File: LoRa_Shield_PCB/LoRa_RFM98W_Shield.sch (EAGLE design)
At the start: 28 parts, among them IC1 AHT10, IC2 TXS0102DCUR, J2 TYPE-C-31-M-17, U1 RFM98W, U2 3V3_REG, X2 BU-SMA-H

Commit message: update
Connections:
- new net N$16: JP5.4
- new net N$8: JP5.3
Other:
- moved on the sheet: C5, C6, IC2, JP5

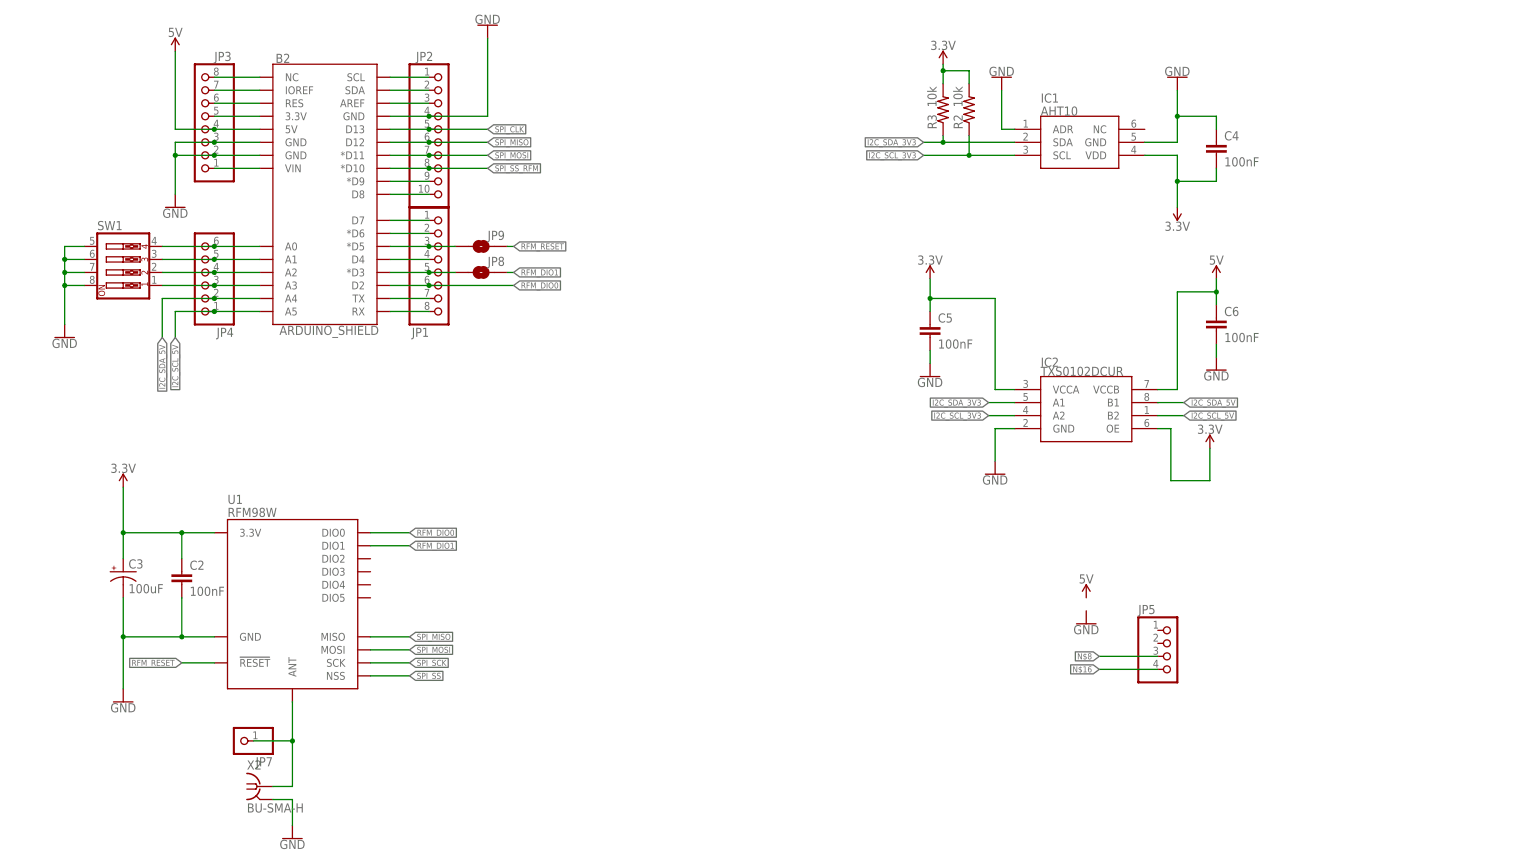
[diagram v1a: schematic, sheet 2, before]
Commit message: ADC circuit, new PCB layout
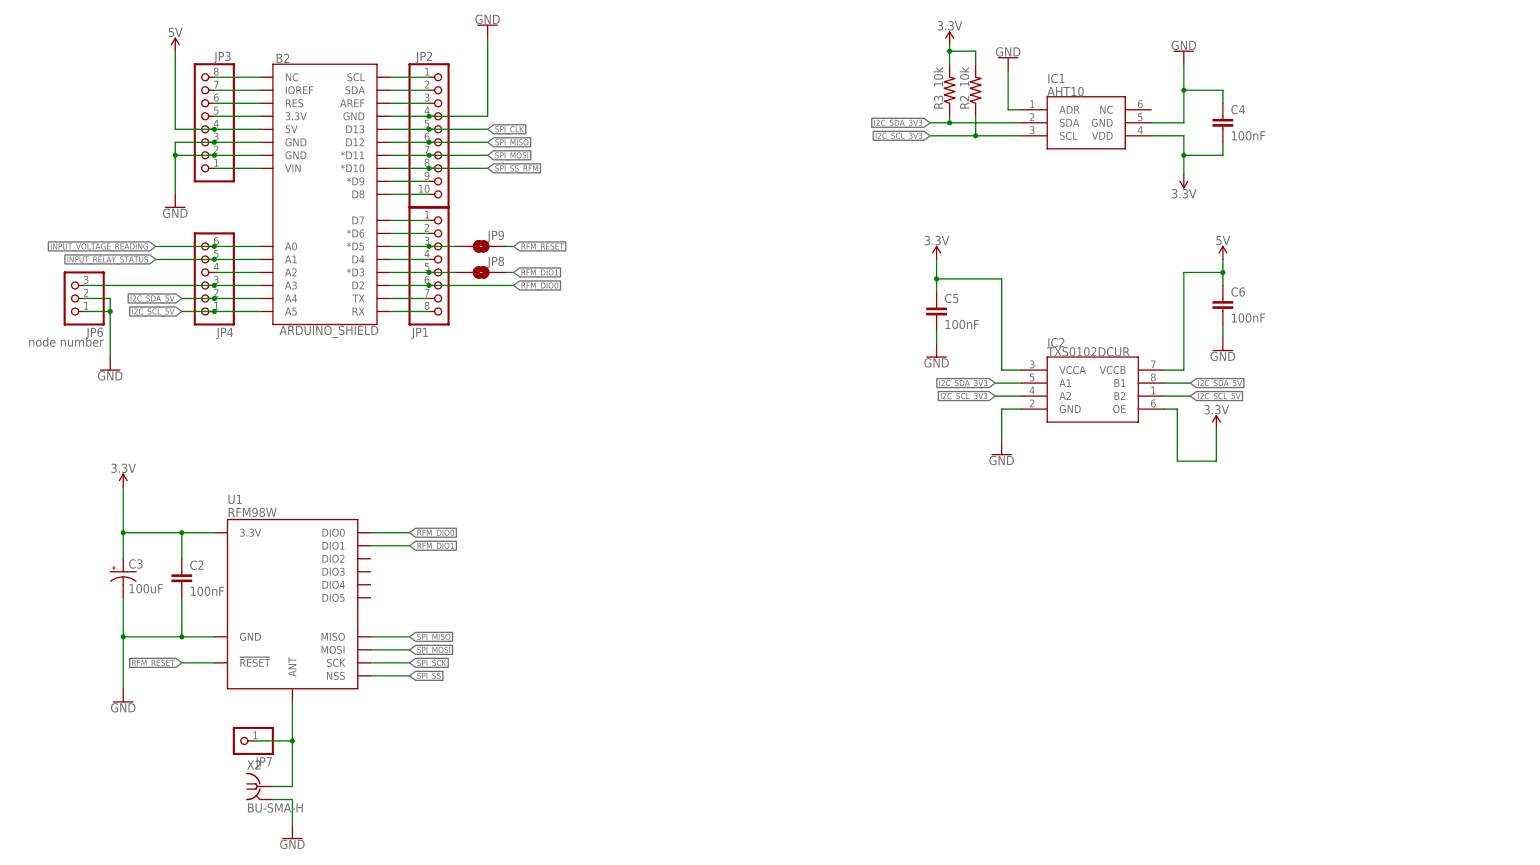
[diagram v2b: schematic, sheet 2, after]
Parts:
- removed SW1: (no value), special:SW_DIP-4
- added C7: 100nF, rcl:C-EUC0603
- added D2, D3: B5819W, dp_devices:DIODE-SOD-123
- added J1: CON_TERMINAL_BLOCK_03-5MM, dp_devices:CON_TERMINAL_BLOCK_03-5MM
- added JP6: node number, pinhead_v2:PINHD-1X3/OCT
- added R5, R7: 10k, rcl:R-US_R0603
- added R6: 150k, rcl:R-US_R0603
- JP5: value (none) -> OLED
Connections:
- removed net N$16: JP5.4
- removed net N$27: B2.A0, JP4.6, SW1.4
- removed net N$28: B2.A1, JP4.5, SW1.3
- new net INPUT_RELAY_STATUS: B2.A1, J1.1, JP4.5, R5.2
- new net INPUT_VOLTAGE_READING: B2.A0, C7.1, D2.A, D3.C, JP4.6, R6.1, R7.2
- net 5V: now also D2.C, JP5.1
- net GND: now also C7.2, D3.A, J1.2, JP5.2, JP6.1, JP6.2, R5.1, R7.1; no longer SW1.5, SW1.6, SW1.7, SW1.8
- net I2C_SCL_5V: now also JP5.3
- net I2C_SDA_5V: now also JP5.4
- net N$29: no longer SW1.2
- net N$30: now also JP6.3; no longer SW1.1
- net N$8: now also J1.3, R6.2; no longer JP5.3
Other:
- moved on the sheet: C1, C10, C4, C5, C6, D1, IC1, IC2, J2, LED1, R1, R2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

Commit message: layout update
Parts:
- removed D2, D3: B5819W, dp_devices:DIODE-SOD-123
- added D4: BAT54SWT1G, SamacSys_Parts:BAT54SWT1G
- added R10, R12, R8: 5k, rcl:R-US_R0603
- added R11, R4, R9: 10k, rcl:R-US_R0603
- R6: value 150k -> 165k
- R7: value 10k -> 15k
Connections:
- removed net SPI_CLK: B2.D13, JP2.5
- removed net SPI_MOSI: B2.*D11, JP2.7, U1.MOSI
- removed net SPI_SCK: U1.SCK
- removed net SPI_SS: U1.NSS
- removed net SPI_SS_RFM: B2.*D10, JP2.8
- new net SPI_CLK_3V3: R4.1, R8.2, U1.SCK
- new net SPI_CLK_5V: B2.D13, JP2.5, R8.1
- new net SPI_MOSI_3V3: R10.2, R9.1, U1.MOSI
- new net SPI_MOSI_5V: B2.*D11, JP2.7, R10.1
- new net SPI_SS_RFM_3V3: R11.1, R12.2, U1.NSS
- new net SPI_SS_RFM_5V: B2.*D10, JP2.8, R12.1
- net 5V: now also D4.CATHODE; no longer D2.C
- net GND: now also D4.ANODE, R11.2, R4.2, R9.2; no longer D3.A
- net INPUT_VOLTAGE_READING: now also D4.CATHODE-ANODE; no longer D2.A, D3.C
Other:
- moved on the sheet: C7, R6

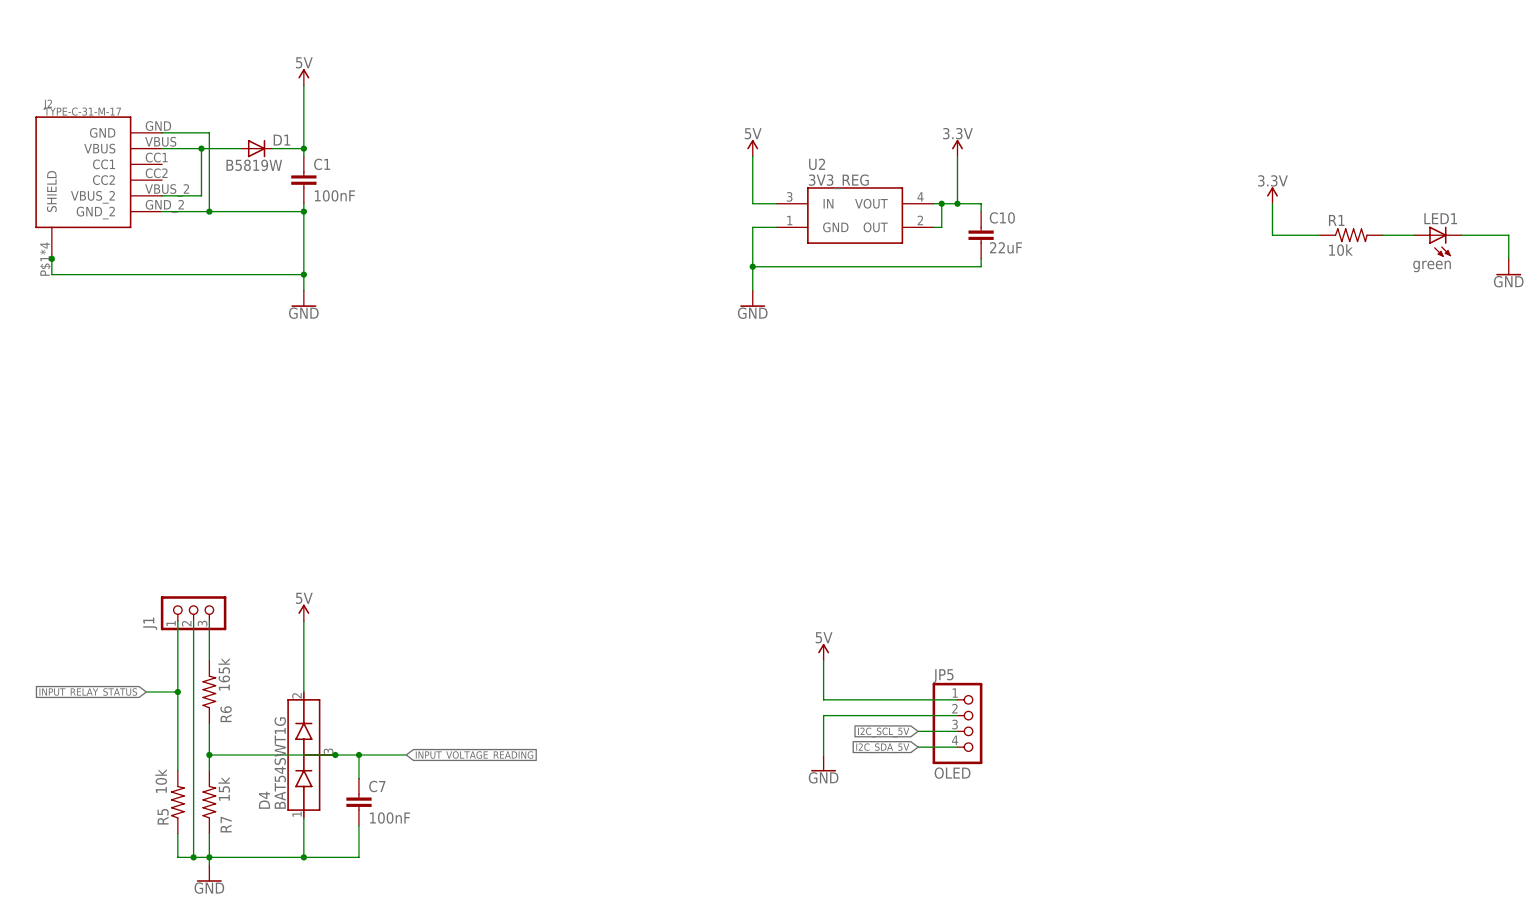
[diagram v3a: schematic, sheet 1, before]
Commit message: schematics, layout update
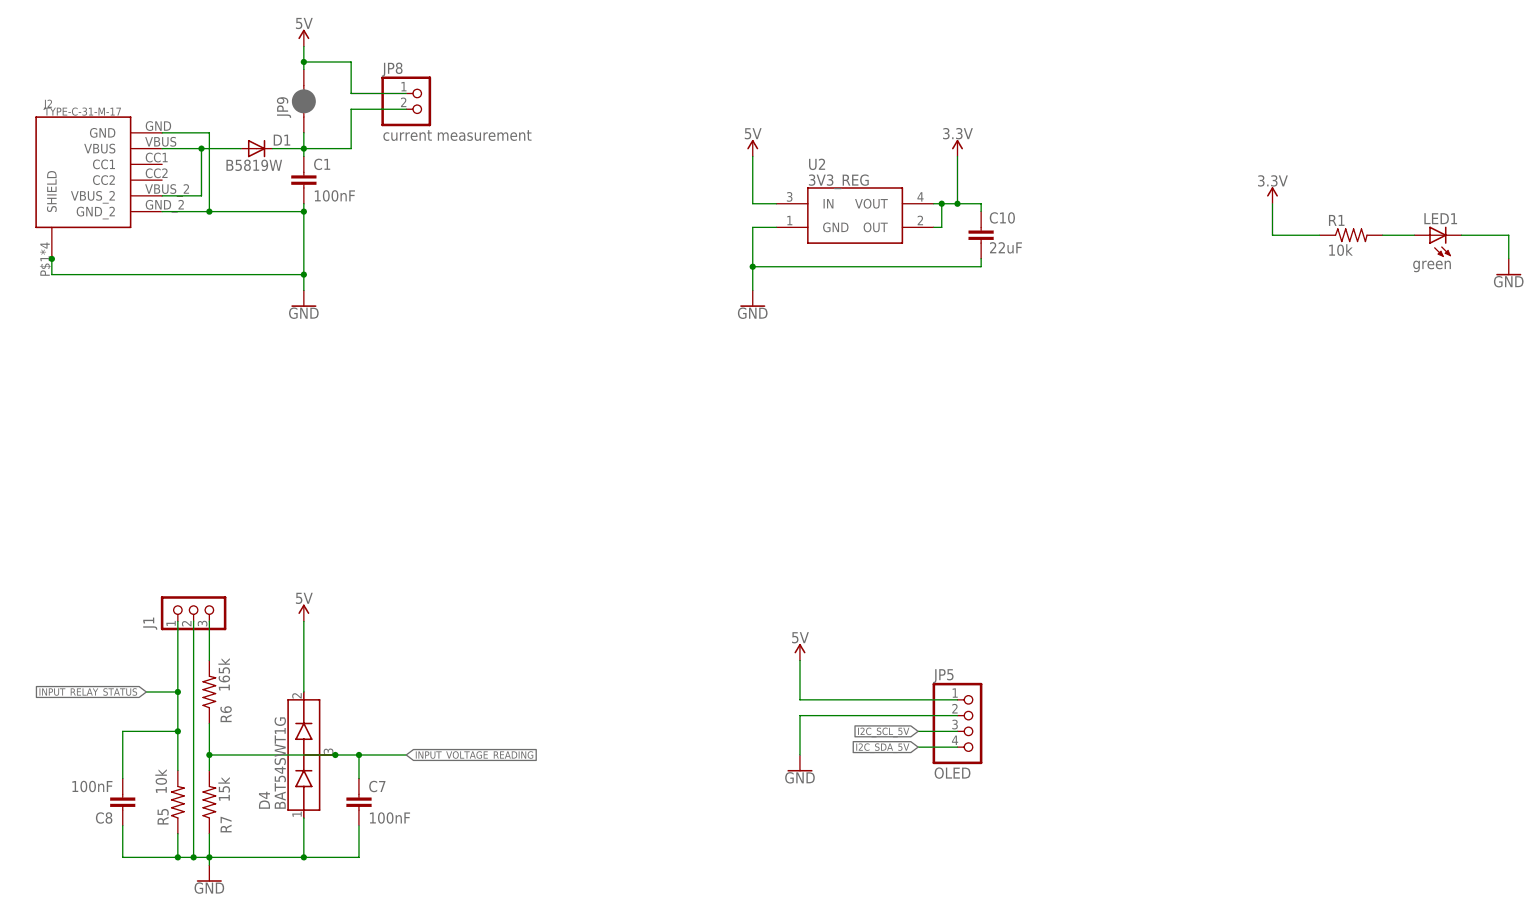
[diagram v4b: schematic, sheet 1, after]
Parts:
- added C8: 100nF, rcl:C-EUC0603
- JP8: value JUMPER-SMT_2_NO_SILK -> current measurement; device SparkFun-Jumpers:JUMPER-SMT_2_NO_SILK -> pinhead_v2:PINHD-1X2/OCT
- JP9: value JUMPER-SMT_2_NO_SILK -> JUMPER-SMT_2_NC_PASTE_SILK; device SparkFun-Jumpers:JUMPER-SMT_2_NO_SILK -> SparkFun-Jumpers:JUMPER-SMT_2_NC_PASTE_SILK
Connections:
- removed net N$11: B2.*D5, JP1.3, JP9.1
- removed net N$9: B2.*D3, JP1.5, JP8.1
- new net N$16: C1.1, D1.C, JP8.2, JP9.1
- net 5V: now also JP8.1, JP9.2; no longer C1.1, D1.C
- net GND: now also C8.1
- net INPUT_RELAY_STATUS: now also C8.2
- net RFM_DIO1: now also B2.*D3, JP1.5; no longer JP8.2
- net RFM_RESET: now also B2.*D5, JP1.3; no longer JP9.2

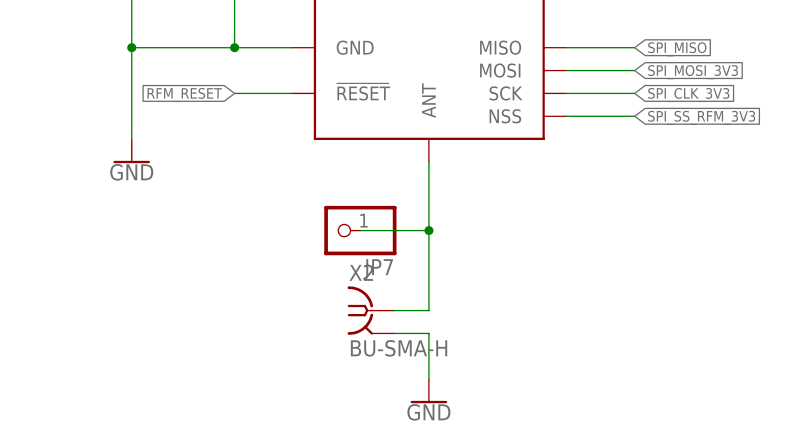
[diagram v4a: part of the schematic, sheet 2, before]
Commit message: PCB routing complete, RF impedance needs work
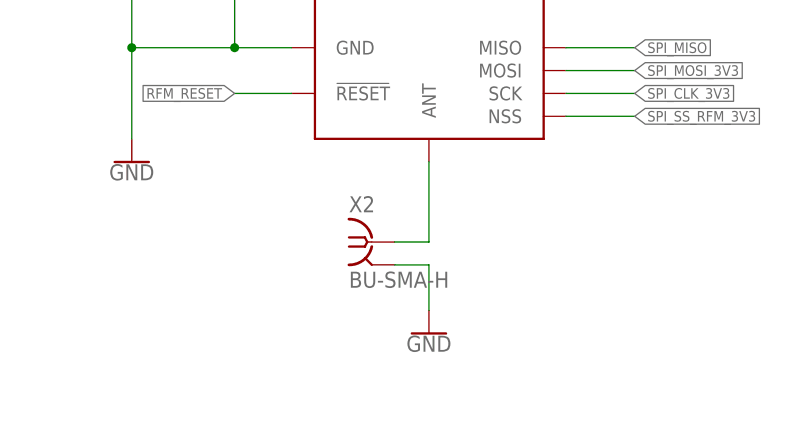
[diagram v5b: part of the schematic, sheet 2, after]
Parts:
- removed JP7: (no value), pinhead_v2:PINHD-1X1/OCT
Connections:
- net N$2: no longer JP7.1
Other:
- moved on the sheet: X2
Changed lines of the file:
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@@
 <setting verticaltext="up"/>
 </settings>
-<grid distance="50" unitdist="mil" unit="mil" style="lines" multiple="1" display="no" altdistance="0.01" altunitdist="inch" altunit="inch"/>
+<grid distance="0.1" unitdist="inch" unit="inch" style="lines" multiple="1" display="no" altdistance="0.01" altunitdist="inch" altunit="inch"/>
 <layers>
 <layer number="1" name="Top" color="4" fill="1" visible="no" active="no"/>
@@
 <part name="JP3" library="pinhead_v2" deviceset="PINHD-1X8" device="/OCT"/>
 <part name="JP4" library="pinhead_v2" deviceset="PINHD-1X6" device="/OCT"/>
-<part name="JP7" library="pinhead_v2" deviceset="PINHD-1X1" device="/OCT"/>
 <part name="X2" library="con-coax" library_urn="urn:adsk.eagle:library:133" deviceset="BU-SMA-H" device="" package3d_urn="urn:adsk.eagle:package:6206/1"/>
 <part name="GND7" library="SparkFun-PowerSymbols" deviceset="GND" device=""/>
@@
 <attribute name="VALUE" x="57.15" y="133.35" size="1.778" layer="96" rot="R180"/>
 </instance>
-<instance part="JP7" gate="A" x="58.42" y="31.75" smashed="yes" rot="R180">
-<attribute name="NAME" x="64.77" y="28.575" size="1.778" layer="95" rot="R180"/>
-<attribute name="VALUE" x="64.77" y="36.83" size="1.778" layer="96" rot="R180"/>
-</instance>
-<instance part="X2" gate="G$1" x="62.23" y="22.86" smashed="yes">
-<attribute name="VALUE" x="59.69" y="17.78" size="1.778" layer="96"/>
-<attribute name="NAME" x="59.69" y="26.162" size="1.778" layer="95"/>
-</instance>
-<instance part="GND7" gate="1" x="68.58" y="12.7" smashed="yes">
-<attribute name="VALUE" x="68.58" y="12.446" size="1.778" layer="96" align="top-center"/>
+<instance part="X2" gate="G$1" x="62.23" y="30.48" smashed="yes">
+<attribute name="VALUE" x="59.69" y="25.4" size="1.778" layer="96"/>
+<attribute name="NAME" x="59.69" y="33.782" size="1.778" layer="95"/>
+</instance>
+<instance part="GND7" gate="1" x="68.58" y="20.32" smashed="yes">
+<attribute name="VALUE" x="68.58" y="20.066" size="1.778" layer="96" align="top-center"/>
 </instance>
 <instance part="GND9" gate="1" x="33.02" y="104.14" smashed="yes">
@@
 <pinref part="X2" gate="G$1" pin="2"/>
 <pinref part="GND7" gate="1" pin="GND"/>
-<wire x1="64.77" y1="20.32" x2="68.58" y2="20.32" width="0.1524" layer="91"/>
-<wire x1="68.58" y1="20.32" x2="68.58" y2="15.24" width="0.1524" layer="91"/>
+<wire x1="64.77" y1="27.94" x2="68.58" y2="27.94" width="0.1524" layer="91"/>
+<wire x1="68.58" y1="27.94" x2="68.58" y2="22.86" width="0.1524" layer="91"/>
 </segment>
 <segment>
@@
 <segment>
 <pinref part="U1" gate="G$1" pin="ANT"/>
-<pinref part="JP7" gate="A" pin="1"/>
-<wire x1="68.58" y1="39.37" x2="68.58" y2="31.75" width="0.1524" layer="91"/>
-<wire x1="68.58" y1="31.75" x2="60.96" y2="31.75" width="0.1524" layer="91"/>
 <pinref part="X2" gate="G$1" pin="1"/>
-<wire x1="64.77" y1="22.86" x2="68.58" y2="22.86" width="0.1524" layer="91"/>
-<wire x1="68.58" y1="22.86" x2="68.58" y2="31.75" width="0.1524" layer="91"/>
-<junction x="68.58" y="31.75"/>
-</segment>
-</net>
+<wire x1="64.77" y1="30.48" x2="68.58" y2="30.48" width="0.1524" layer="91"/>
+<wire x1="68.58" y1="30.48" x2="68.58" y2="39.37" width="0.1524" layer="91"/>
+</segment>
+</net>
